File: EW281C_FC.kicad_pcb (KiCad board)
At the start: 4 copper layers, 37.1 x 37.2 mm, 121 parts, among them J1 Conn_01x02, J10 Conn_01x08, J11 Conn_01x03, J12 Conn_01x02, J13 USB_B_Micro, J14 Conn_01x04, J15 Conn_01x04, J16 Conn_01x01, J17 Conn_01x04, J2 Conn_01x04, J3 Conn_01x04, J4 Conn_01x03, J5 Conn_01x03, J6 Conn_01x06, J7 Conn_01x06, J8 Conn_01x04, J9 Conn_01x08, Q1 BSS138, SW1 SW_Push, U1 LP2985-3.3, U10 W25Q128JVS, U2 STM32F722RETx, U3 LP2985-3.3, U4 MP4560_QFN10, U5 MP4560_QFN10, U6 MAX7456EUI+, U7 MPU-6000, U9 BMP388, Y1 27MHz

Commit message: Small cleanups
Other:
- board text added: "4V5"
- board text removed: "Probably don’t need resistor"
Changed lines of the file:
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@@
   (general
     (thickness 1.6)
-    (drawings 145)
+    (drawings 144)
     (tracks 919)
     (zones 0)
@@
   (layers
     (0 F.Cu power)
-    (1 In1.Cu power hide)
-    (2 In2.Cu power hide)
-    (31 B.Cu power hide)
+    (1 In1.Cu power)
+    (2 In2.Cu power)
+    (31 B.Cu power)
     (32 B.Adhes user hide)
     (33 F.Adhes user hide)
@@
     (44 Edge.Cuts user)
     (45 Margin user hide)
-    (46 B.CrtYd user hide)
+    (46 B.CrtYd user)
     (47 F.CrtYd user)
     (48 B.Fab user hide)
@@
   (module Footprints:BMP388 (layer F.Cu)
     (at 103.07 99.55 180)
-    (fp_text reference U9 (at -0.284383 -1.605376) (layer F.SilkS)
+    (fp_text reference U9 (at -0.284383 -1.605376) (layer B.Fab)
       (effects (font (size 0.320434 0.320434) (thickness 0.015)))
     )
@@
     (fp_line (start 2.66 -1.12) (end 2.66 1.12) (layer F.CrtYd) (width 0.05))
     (fp_line (start 2.66 1.12) (end -2.66 1.12) (layer F.CrtYd) (width 0.05))
-    (fp_text user "Copyright 2016 Accelerated Designs. All rights reserved." (at 0 0 90) (layer Cmts.User)
-      (effects (font (size 0.127 0.127) (thickness 0.002)))
-    )
     (fp_text user * (at -2.54 0 90) (layer F.SilkS)
       (effects (font (size 1 1) (thickness 0.15)))
@@
     (fp_line (start 2.66 -1.12) (end 2.66 1.12) (layer F.CrtYd) (width 0.05))
     (fp_line (start 2.66 1.12) (end -2.66 1.12) (layer F.CrtYd) (width 0.05))
-    (fp_text user "Copyright 2016 Accelerated Designs. All rights reserved." (at 0 0 90) (layer Cmts.User)
-      (effects (font (size 0.127 0.127) (thickness 0.002)))
-    )
     (fp_text user * (at -2.54 0 90) (layer F.SilkS)
       (effects (font (size 1 1) (thickness 0.15)))
@@
   (module JPW_Footprints:MAX7456EUI&plus_T (layer F.Cu)
     (at 104.03 83.78)
-    (fp_text reference U6 (at 0 0) (layer F.SilkS)
+    (fp_text reference U6 (at 0 0) (layer F.Fab)
       (effects (font (size 1 1) (thickness 0.15)))
     )
@@
     (fp_line (start -2.5019 4.6568) (end -3.8608 4.6568) (layer F.CrtYd) (width 0.05))
     (fp_arc (start 0 -4.9022) (end 0.3048 -4.9022) (angle 180) (layer F.Fab) (width 0.1524))
-    (fp_text user "Copyright 2016 Accelerated Designs. All rights reserved." (at 0 0) (layer Cmts.User)
-      (effects (font (size 0.127 0.127) (thickness 0.002)))
-    )
     (pad 29 smd rect (at 0 0) (size 3.0988 6.9088) (layers F.Cu F.Paste F.Mask)
       (net 1 GND))
@@
     (tags "DFN NoLead")
     (attr smd)
-    (fp_text reference U5 (at 0 2.45 90) (layer B.SilkS)
+    (fp_text reference U5 (at 0 2.45 90) (layer B.Fab)
       (effects (font (size 1 1) (thickness 0.15)) (justify mirror))
     )
@@
     (tags "DFN NoLead")
     (attr smd)
-    (fp_text reference U4 (at 0 2.45 90) (layer B.SilkS)
+    (fp_text reference U4 (at 0 2.45 90) (layer B.Fab)
       (effects (font (size 1 1) (thickness 0.15)) (justify mirror))
     )
@@
     (effects (font (size 0.6 0.6) (thickness 0.15)) (justify mirror))
   )
-  (gr_text 5V (at 81.475 80.595 270) (layer B.SilkS)
+  (gr_text 4V5 (at 81.475 80.595 270) (layer B.SilkS)
     (effects (font (size 0.6 0.6) (thickness 0.15)) (justify mirror))
   )
@@
     (effects (font (size 0.6 0.6) (thickness 0.15)) (justify mirror))
   )
-  (gr_text 5V (at 81.475 80.465 270) (layer F.SilkS)
+  (gr_text 4V5 (at 81.475 80.465 270) (layer F.SilkS)
     (effects (font (size 0.6 0.6) (thickness 0.15)))
   )
@@
     (arrow2b (pts (xy 113.56 90.06) (xy 112.973579 88.933496)))
   )
-  (gr_text "Probably don’t need resistor" (at 95.46 88.92) (layer Cmts.User)
-    (effects (font (size 0.1 0.1) (thickness 0.025)) (justify mirror))
-  )
   (gr_line (start 114.479862 104.890094) (end 114.48 78.12) (layer Edge.Cuts) (width 0.1))

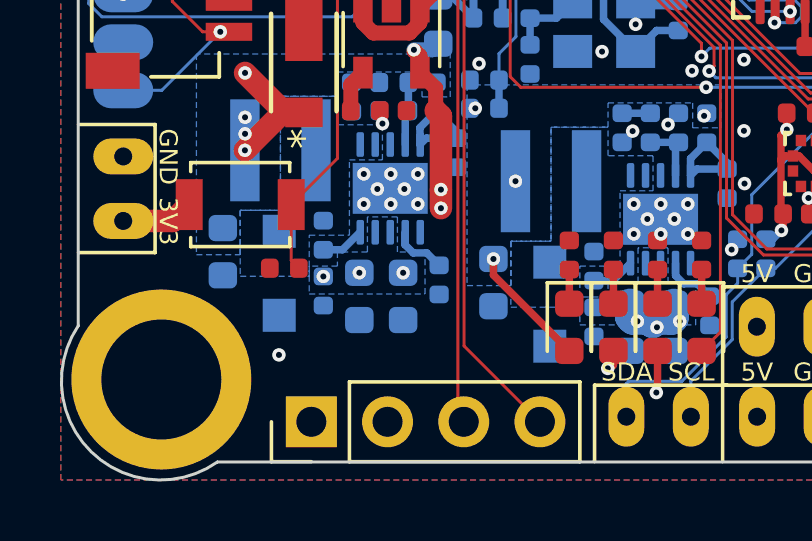
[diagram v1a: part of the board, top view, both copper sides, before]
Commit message: Added trace for 3V3
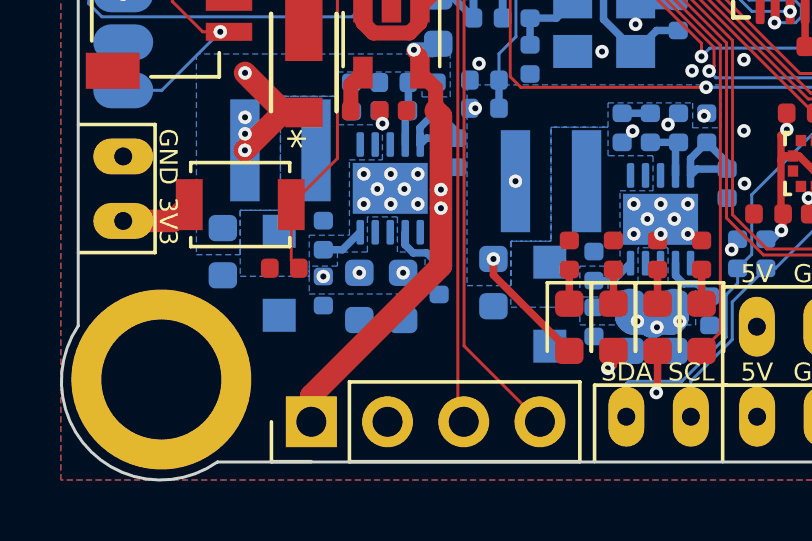
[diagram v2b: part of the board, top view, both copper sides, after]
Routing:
- net +3V3: track 44.7 -> 53.6 mm, vias 22 -> 21

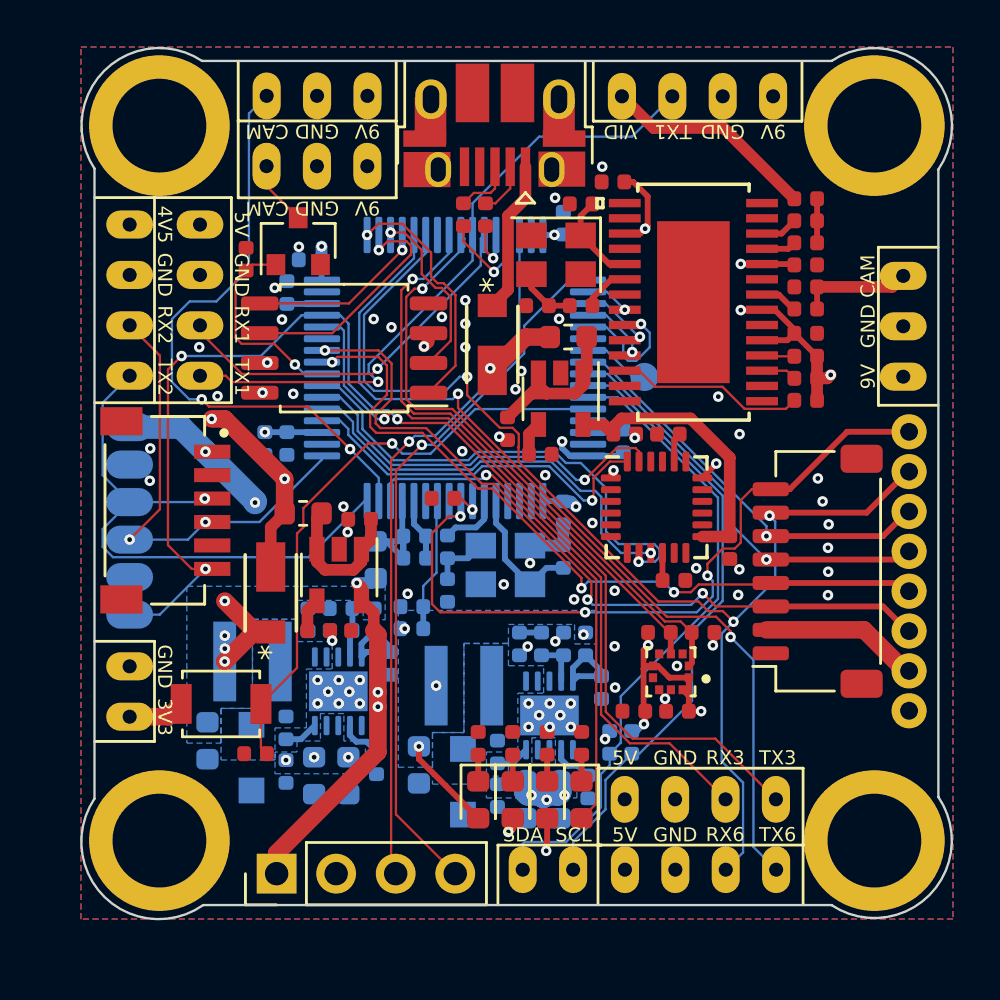
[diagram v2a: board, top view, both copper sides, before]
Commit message: Added LED for VCC
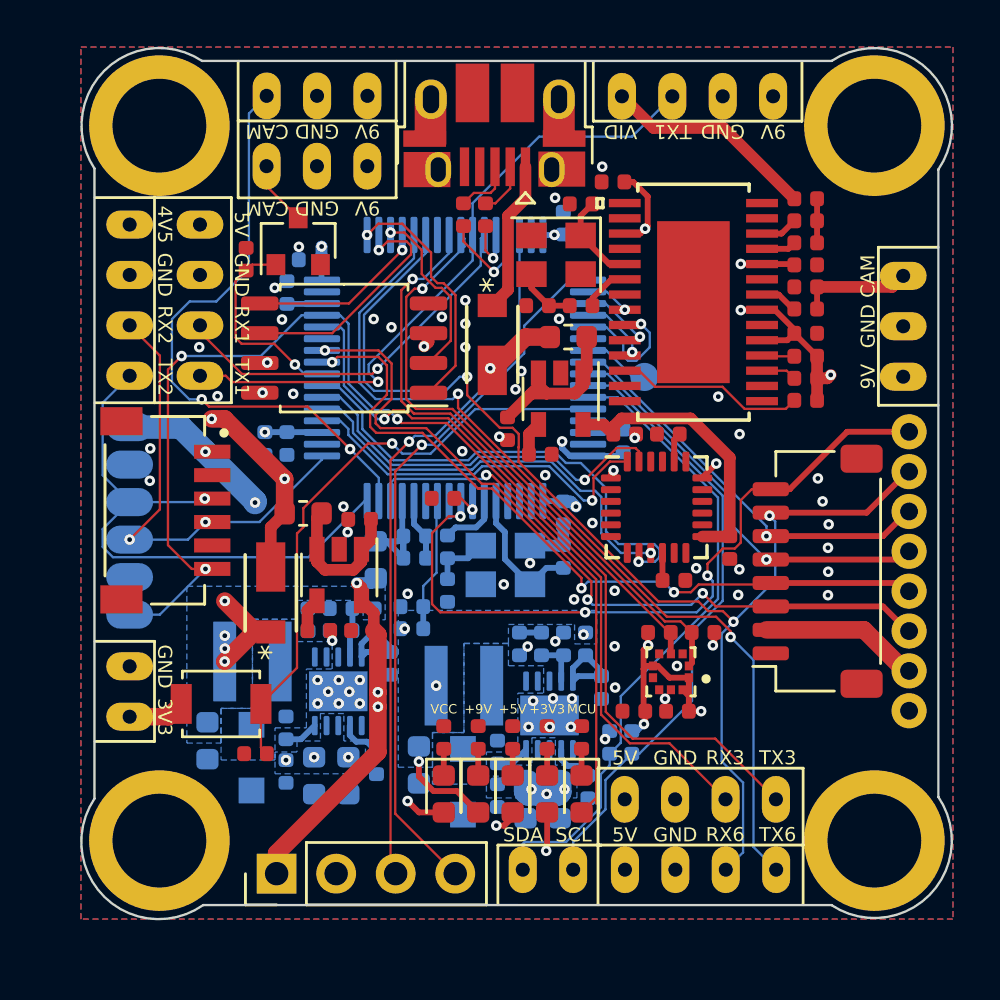
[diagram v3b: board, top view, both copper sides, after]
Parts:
- added D9: PURPLE, LED_SMD:LED_0603_1608Metric, F.Cu at (93.4, 104.8)
- added R9: 1k, Resistor_SMD:R_0402_1005Metric, F.Cu at (93.4, 102.3)
- moved D3 0.25 mm to (97.8, 104.8)
- moved D5 0.25 mm to (99.3, 104.8)
- moved D7 0.25 mm to (96.3, 104.8)
- moved D8 0.25 mm to (94.8, 104.8)
- moved R21 0.25 mm to (97.8, 102.3)
- moved R23 0.25 mm to (99.3, 102.3)
- moved R26 0.25 mm to (96.3, 102.3)
- moved R28 0.25 mm to (94.8, 102.3)
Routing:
- net VCC: track 48.2 -> 50.0 mm, vias 7 -> 8
- net Net-(D9-Pad1): track 0.00 -> 1.14 mm
- net GND: vias 67 -> 65
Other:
- board text added: "+3V3"
- board text added: "+5V"
- board text added: "+9V"
- board text added: "MCU"

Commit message: Added logos
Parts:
- added G***: LOGO, Footprints:USN, B.Cu at (105.7, 86.2)
- added G***: LOGO, Footprints:EGA, B.Cu at (105.4, 97.3)

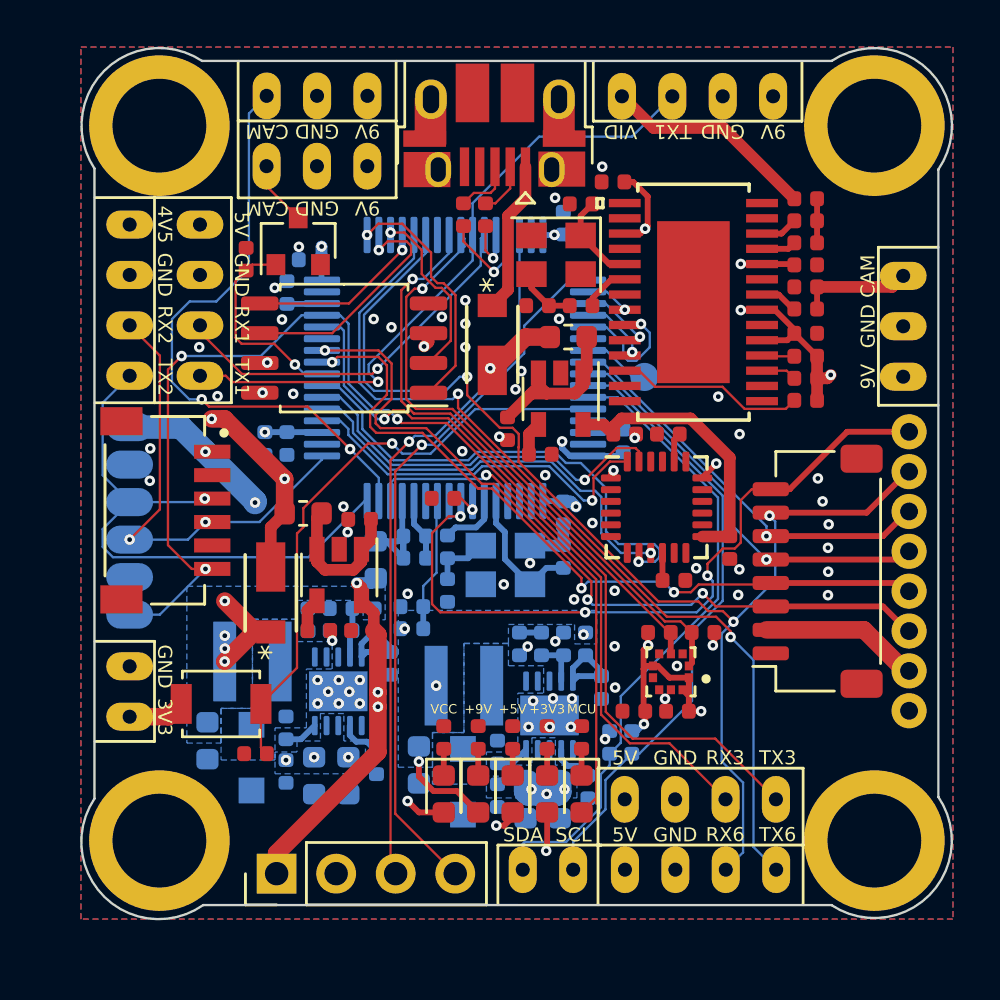
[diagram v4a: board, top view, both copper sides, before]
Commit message: Changed to 20x20 form factor
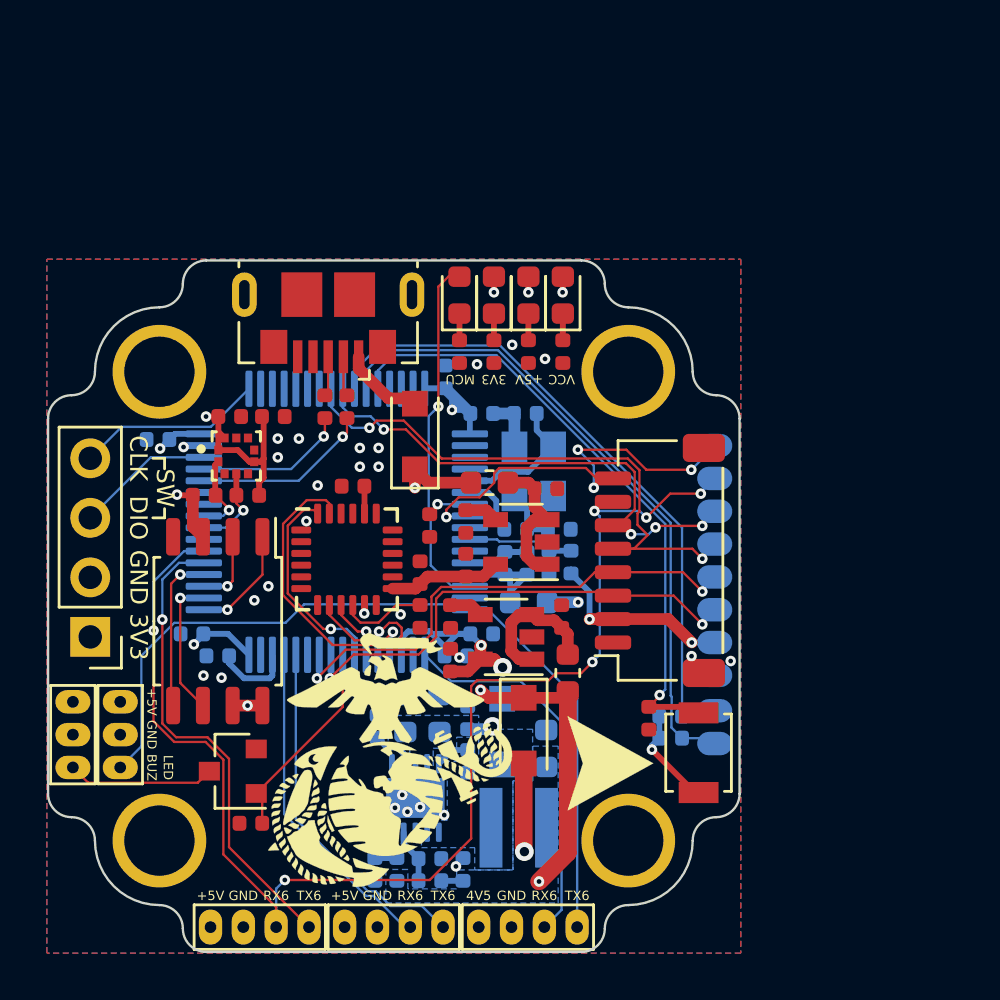
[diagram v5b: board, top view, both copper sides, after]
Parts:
- removed C20, C28, C39, C40, C41, C42: 0.1uF, Capacitor_SMD:C_0402_1005Metric
- removed C22: 22uF, Capacitor_SMD:C_0603_1608Metric
- removed C24, C27: 2.2uF, Capacitor_SMD:C_0603_1608Metric
- removed C33: 560pF, Capacitor_SMD:C_0402_1005Metric
- removed C35: 1pF, Capacitor_SMD:C_0402_1005Metric
- removed C37, C38: 10uF, Capacitor_SMD:C_0402_1005Metric
- removed C43, C44: 10pF, Capacitor_SMD:C_0402_1005Metric
- removed D4: 90V, 2A, Diode_SMD:D_SOD-123F
- removed D8: GREEN, LED_SMD:LED_0603_1608Metric
- removed G***: LOGO, Footprints:USN
- removed G***: LOGO, Footprints:EGA
- removed J1: Conn_01x02, Connector_Wire:SolderWire-0.1sqmm_1x02_P3.6mm_D0.4mm_OD1mm
- removed J13: USB_B_Micro, Connector_USB:USB_Micro-B_Amphenol_10103594-0001LF_Horizontal
- removed J15, J17: Conn_01x04, Connector_Wire:SolderWire-0.1sqmm_1x04_P3.6mm_D0.4mm_OD1mm
- removed J16: Conn_01x01, Connector_Wire:SolderWire-0.1sqmm_1x01_D0.4mm_OD1mm
- removed J6: Conn_01x06, Footprints:JST_SM06B-SRSS-TB(LF)(SN)
- removed J7: Conn_01x06, Connector_Wire:Connector_Wire_Solder_DJI
- removed L1: 15uH, Inductor_SMD:L_XGL4030
- removed R10: 20k, Resistor_SMD:R_0402_1005Metric
- removed R12: 2k, Resistor_SMD:R_0402_1005Metric
- removed R17: 200k, Resistor_SMD:R_0402_1005Metric
- removed R22: 120k, Resistor_SMD:R_0402_1005Metric
- removed R25, R29, R30: 1k, Resistor_SMD:R_0402_1005Metric
- removed R28: 233, Resistor_SMD:R_0402_1005Metric
- removed R33, R34: 75, Resistor_SMD:R_0402_1005Metric
- removed R35: 589, Resistor_SMD:R_0402_1005Metric
- removed U4: MP4560_QFN10, Package_DFN_QFN:DFN-10-1EP_3x3mm_P0.5mm_EP1.7x2.5mm
- removed U6: MAX7456EUI+, JPW_Footprints:MAX7456EUI&plus_T
- removed Y1: 27MHz, Oscillator:Oscillator_SMD_Abracon_ASE-4Pin_3.2x2.5mm
- added L3: USN, Footprints:USN, B.Cu at (86.4, 103.4)
- added L4: EGA, Footprints:EGA, F.Cu at (91.1, 103.3)
- added L5: Arrow, Footprints:Arrow, F.Cu at (100.5, 103.5)
- D1, D2: value D_Schottky -> 90V, 2A; footprint Footprints:SBR3U30P1-7 -> Diode_SMD:D_SOD-123F
- H1, H2, H3, H4: footprint MountingHole:MountingHole_2.7mm_Pad -> MountingHole:MountingHole_3mm_M2_20x20
- J10: footprint Connector_Wire:SolderWire-0.1sqmm_1x08_D0.4mm_OD1mm -> Connector_Wire:Conn_FC_Solder_8; moved to B.Cu
- J11, J4: footprint Connector_Wire:SolderWire-0.1sqmm_1x03_P3.6mm_D0.4mm_OD1mm -> Connector_Wire:Conn_3Pin
- J12: footprint Connector_Wire:SolderWire-0.1sqmm_1x02_P3.6mm_D0.4mm_OD1mm -> Connector_Wire:Conn_2Pin; moved to B.Cu
- J14, J2, J3: footprint Connector_Wire:SolderWire-0.1sqmm_1x04_P3.6mm_D0.4mm_OD1mm -> Connector_Wire:Conn_4Pin
- J5: value Conn_01x03 -> USB_B_Micro; footprint Connector_Wire:SolderWire-0.1sqmm_1x03_P3.6mm_D0.4mm_OD1mm -> Connector_USB:USB_Micro-B_GCT_USB3076-30-A
- moved H3 32.3 mm to (101.2, 106.8)
- moved J14 31.7 mm to (97.0, 110.4), turned to 0 degrees
- moved J11 28.5 mm to (79.6, 102.2), turned to 270 degrees
- moved J4 26.4 mm to (77.6, 102.2), turned to 270 degrees
- moved J5 24.5 mm to (88.5, 84.7), turned to 180 degrees
- moved R1 24.1 mm to (85.2, 106.0), turned to 180 degrees
- moved C10 22.9 mm to (84.2, 88.7), turned to 0 degrees
- moved Q1 22.8 mm to (84.4, 103.8), turned to 180 degrees
- moved H2 22.6 mm to (101.2, 86.8)
- moved R5 22.1 mm to (83.2, 92.0), turned to 180 degrees
- moved D5 21.9 mm to (94.0, 83.5), turned to 90 degrees
- moved D9 21.9 mm to (98.5, 83.5), turned to 90 degrees
- moved D3 21.4 mm to (95.5, 83.5), turned to 90 degrees
- moved D7 21.3 mm to (97.0, 83.5), turned to 90 degrees
- moved U9 20.7 mm to (84.5, 90.3), turned to 0 degrees
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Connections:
- J5 pad 1: +9V -> +5V_USB
- J5 pad 2: GND -> /Connectors/USB_D-
- J5 pad 3: /CAM -> /Connectors/USB_D+
- R15 pad 1: /MCU/USB_D+ -> /Connectors/USB_D+
- R7 pad 1: /MCU/USB_D- -> /Connectors/USB_D-
- U2 pad 20: /MCU/SPI1_CS -> /Gyro/SPI1_CS
- U2 pad 21: /Gyro/SPI1_MISO -> /Gyro/SPI1_SCK
- U2 pad 22: /MCU/SPI1_MISO -> /Gyro/SPI1_MISO
- U2 pad 23: /Gyro/SPI1_CS -> /Gyro/SPI1_MOSI
- U2 pad 25: /Connectors/M2 -> /Connectors/M1
- U2 pad 26: /Connectors/M1 -> /Connectors/M2
- U2 pad 42: /Connectors/UART1_TX -> (no net)
- U2 pad 43: /Connectors/UART1_RX -> (no net)
- U2 pad 50: /MCU/SPI3_CS -> (no net)
- U2 pad 51: /MCU/SPI3_SCK -> (no net)
- U2 pad 52: /MCU/SPI3_MISO -> (no net)
- U2 pad 53: /MCU/SPI3_MOSI -> (no net)
- U2 pad 55: /Connectors/SWO -> (no net)
- U2 pad 56: /Connectors/M4 -> /Connectors/M3
- U2 pad 57: /Connectors/M3 -> /Connectors/M4
- U7 pad 23: /MCU/SPI1_MISO -> /Gyro/SPI1_SCK
- U7 pad 24: /MCU/SPI1_CS -> /Gyro/SPI1_MOSI
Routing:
- net +9V: track 65.0 -> 0.00 mm, vias 5 -> 0
- net /Connectors/UART3_RX: track 52.1 -> 14.2 mm, vias 3 -> 0
- net /Connectors/UART1_TX: track 27.7 -> 0.00 mm, vias 1 -> 0
- net /Connectors/SWDIO: track 30.1 -> 5.91 mm, vias 1 -> 0
- net /Barometer/I2C3_SCL: track 26.1 -> 3.54 mm
- net /Connectors/SWCLK: track 30.5 -> 8.00 mm, vias 1 -> 0
- net /Barometer/I2C3_SDA: track 24.7 -> 3.67 mm
- net /Connectors/UART6_TX: track 39.0 -> 20.3 mm, vias 2 -> 1
- net /Connectors/UART3_TX: track 32.8 -> 15.2 mm, vias 1 -> 0
- net /MCU/SPI1_MISO: track 16.7 -> 0.00 mm, vias 1 -> 0
- net VCC: track 50.0 -> 33.5 mm, vias 8 -> 4
- net /Connectors/UART1_RX: track 16.3 -> 0.00 mm, vias 1 -> 0
- net /MCU/SPI1_CS: track 16.1 -> 0.00 mm, vias 1 -> 0
- net /Gyro/SPI1_CS: track 20.8 -> 4.77 mm
- net /Gyro/SPI1_MISO: track 18.0 -> 2.78 mm
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- removed copper zone on B.Cu, net +9V
- removed copper zone on B.Cu, net Net-(C20-Pad2)
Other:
- board size 37.1 x 37.2 mm -> 29.5 x 29.5 mm
- board text added: "BUZ"
- board text added: "CLK"
- board text added: "CURR"
- board text added: "DIO"
- board text added: "EW281C Prof DeVries LCDR Elsberry MIDN 1/C Wolfe"
- board text added: "LED"
- board text added: "SW"
- board text removed: "+3V3"
- board text removed: "+9V"
- board text removed: "5V"
- board text removed: "9V"
- board text removed: "CAM"
- board text removed: "CUR"
- board text removed: "RX1"
- board text removed: "RX2"
- board text removed: "RX3"
- board text removed: "SCL"
- board text removed: "SDA"
- board text removed: "TX1"
- board text removed: "TX2"
- board text removed: "TX3"
- board text removed: "VID"
